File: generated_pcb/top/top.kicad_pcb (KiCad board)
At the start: 2 copper layers, 114.5 x 89 mm, 0 parts

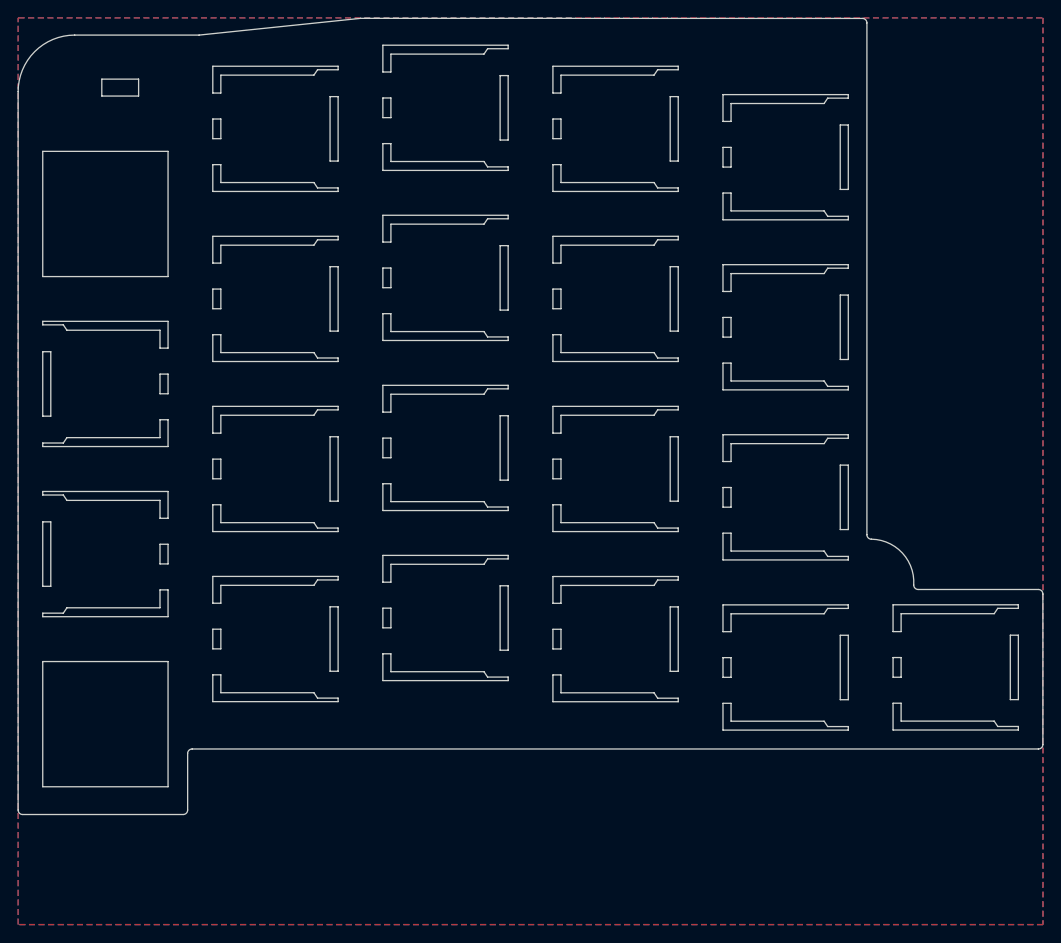
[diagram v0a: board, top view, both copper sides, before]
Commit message: feat: completed the new approach of generating PCBs from the master
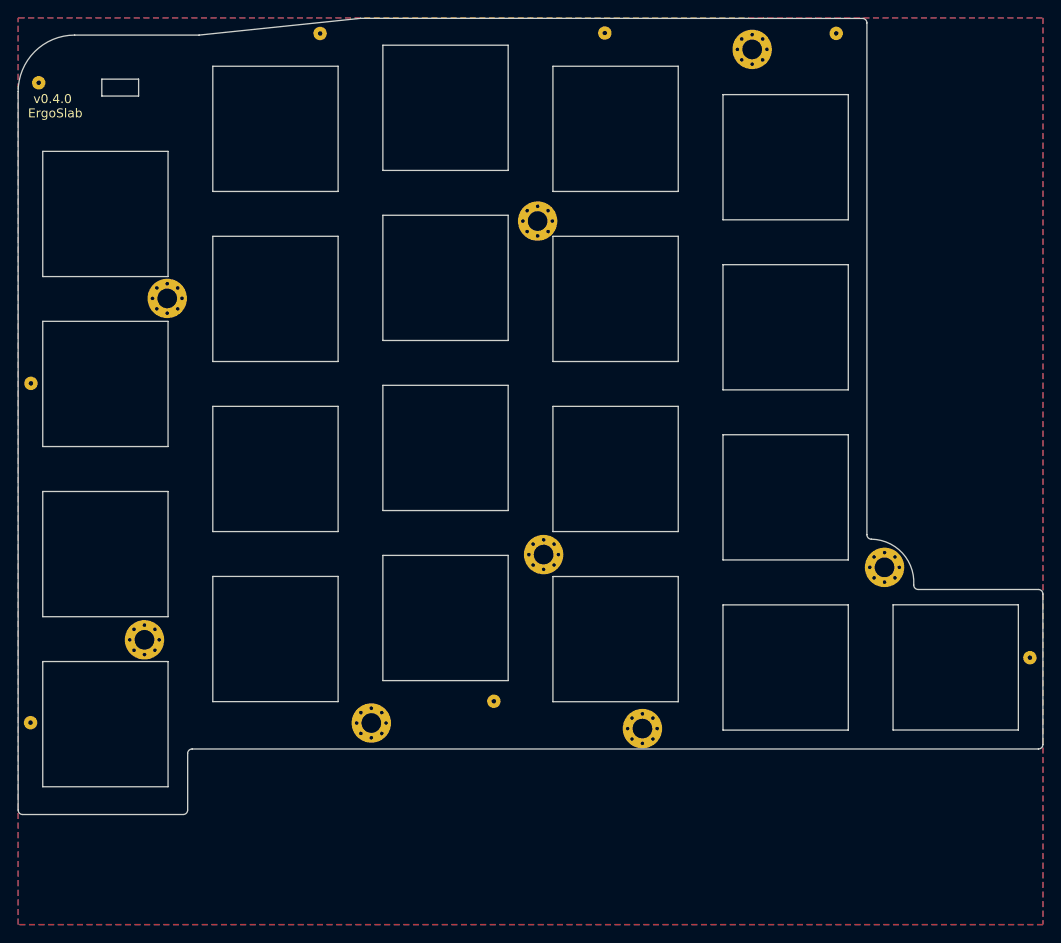
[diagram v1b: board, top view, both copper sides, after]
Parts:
- added Brace0: switchplate-brace, footprints:switchplate-brace, F.Cu at (73.8, 122.9)
- added Brace1: switchplate-brace, footprints:switchplate-brace, F.Cu at (73.9, 85.0)
- added Brace2: switchplate-brace, footprints:switchplate-brace, F.Cu at (74.8, 51.4)
- added Brace3: switchplate-brace, footprints:switchplate-brace, F.Cu at (106.2, 45.9)
- added Brace4: switchplate-brace, footprints:switchplate-brace, F.Cu at (138.0, 45.8)
- added Brace5: switchplate-brace, footprints:switchplate-brace, F.Cu at (163.8, 45.9)
- added Brace6: switchplate-brace, footprints:switchplate-brace, F.Cu at (185.5, 115.6)
- added Brace7: switchplate-brace, footprints:switchplate-brace, F.Cu at (125.6, 120.5)
- added Mount0: MountingHole_2.2mm_M2_Pad_Via, MountingHole:MountingHole_2.2mm_M2_Pad_Via, F.Cu at (154.5, 47.7)
- added Mount1: MountingHole_2.2mm_M2_Pad_Via, MountingHole:MountingHole_2.2mm_M2_Pad_Via, F.Cu at (89.1, 75.5)
- added Mount2: MountingHole_2.2mm_M2_Pad_Via, MountingHole:MountingHole_2.2mm_M2_Pad_Via, F.Cu at (130.5, 66.8)
- added Mount3: MountingHole_2.2mm_M2_Pad_Via, MountingHole:MountingHole_2.2mm_M2_Pad_Via, F.Cu at (86.6, 113.6)
- added Mount4: MountingHole_2.2mm_M2_Pad_Via, MountingHole:MountingHole_2.2mm_M2_Pad_Via, F.Cu at (131.2, 104.1)
- added Mount5: MountingHole_2.2mm_M2_Pad_Via, MountingHole:MountingHole_2.2mm_M2_Pad_Via, F.Cu at (169.2, 105.5)
- added Mount6: MountingHole_2.2mm_M2_Pad_Via, MountingHole:MountingHole_2.2mm_M2_Pad_Via, F.Cu at (111.9, 122.9)
- added Mount7: MountingHole_2.2mm_M2_Pad_Via, MountingHole:MountingHole_2.2mm_M2_Pad_Via, F.Cu at (142.2, 123.5)
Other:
- outline, holes or cut-outs redrawn
- board text added: "ErgoSlab"
- board text added: "v0.4.0"

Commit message: chore: bump version to 1.0.0 now I know it works (typing on it right now), give OLED resistor more space, make choc row M2 mounts more obvious, fix up silk screen build instructions
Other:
- board text added: "v1.0.0"
- board text removed: "v0.4.0"
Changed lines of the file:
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@@
   (title_block
     (title ErgoSlab)
-    (rev 0.4.0)
+    (rev 1.0.0)
     (company "By Tom Saleeba")
     (comment 1 "MIT License")
@@
     (effects (font (size 1 1) (thickness 0.1501)))
   )
-  (gr_text v0.4.0 (at 76.3 53.2) (layer F.SilkS)
+  (gr_text v1.0.0 (at 76.3 53.2) (layer F.SilkS)
     (effects (font (size 1 1) (thickness 0.1501)))
   )
